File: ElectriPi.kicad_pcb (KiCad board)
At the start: 2 copper layers, 65 x 56 mm, 57 parts, among them IC2 TPS51397ARJER, J1 282837-2, J2 JST XH 01x02, J3 JST XH 01x02, J6 Raspberry_Pi_2_3, J8 JST XH 01x02, Q1 SiA471DJ, Q2 SiA430DJT, U1 LM74700, U2 COOLING, U3 TVS0500DRV

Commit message: Fix libraries and updated back silk
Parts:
- G***: value LOGO -> V3D Logo Small; footprint LOGO -> Logos:V3D Logo Small

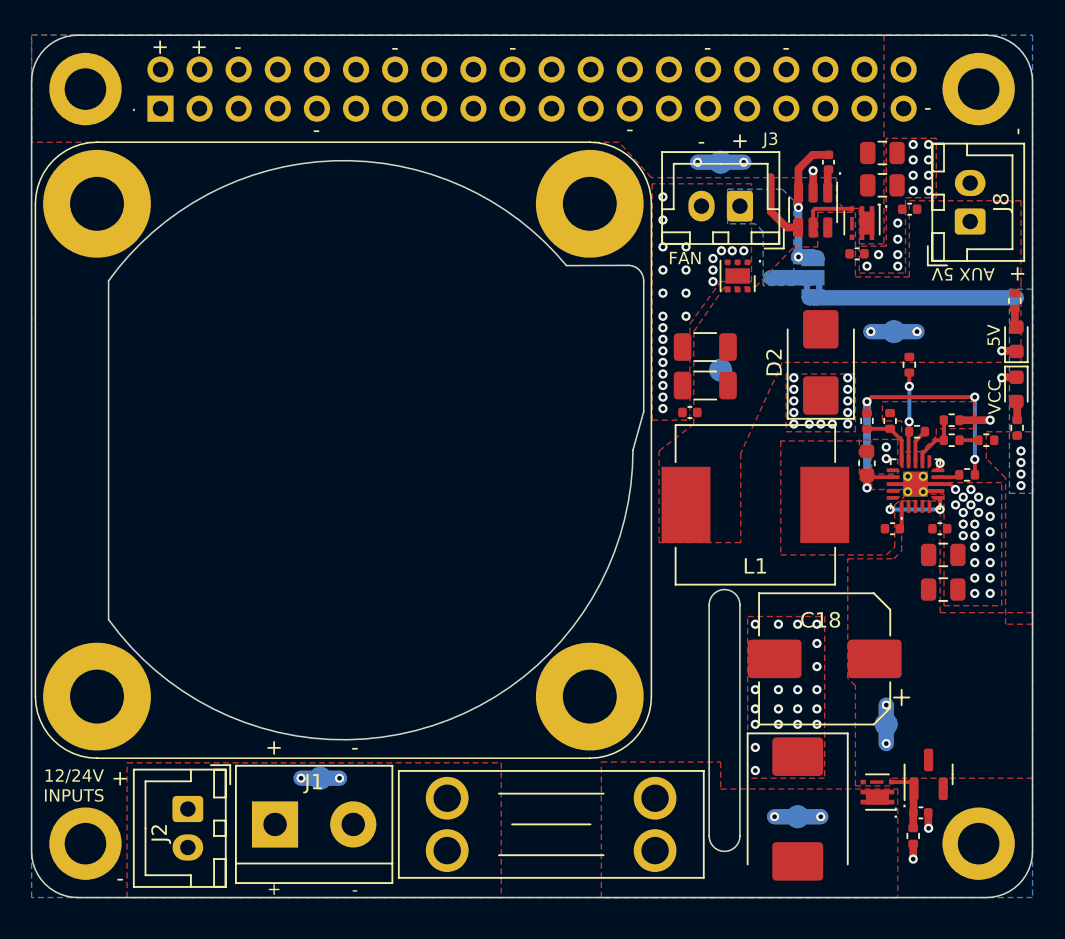
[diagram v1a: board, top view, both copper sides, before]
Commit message: Remove JST input / output connectors! Not rated for currents
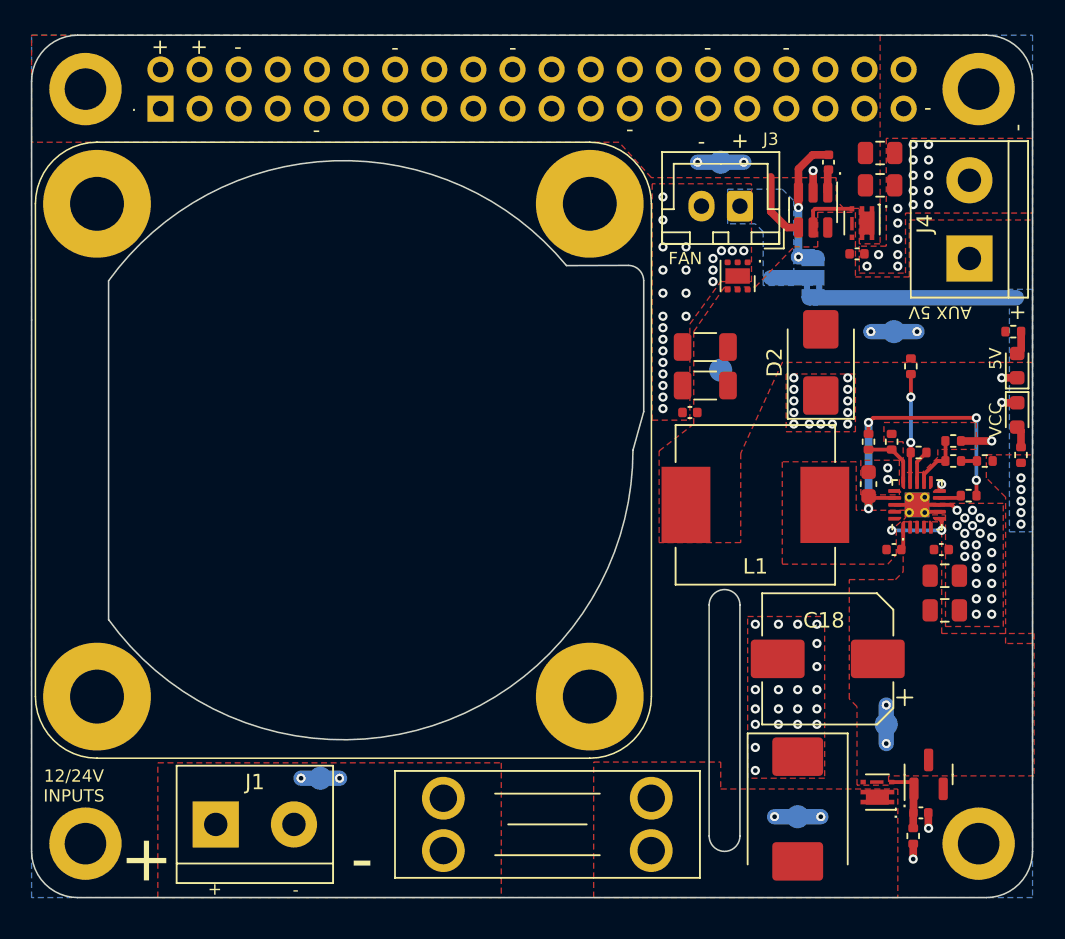
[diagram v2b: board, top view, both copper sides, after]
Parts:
- removed C15: 0.1uF, Capacitor_SMD:C_0402_1005Metric
- removed J2, J8: JST XH 01x02, Connector_JST:JST_XH_B2B-XH-A_1x02_P2.50mm_Vertical
- added J4: 282837-2, TerminalBlock:TerminalBlock_bornier-2_P5.08mm, F.Cu at (146.2, 67.8)
- moved J1 3.85 mm to (97.2, 104.5)
- moved R6 2.00 mm to (149.0, 72.5), turned to 180 degrees
- moved R8 1.78 mm to (149.5, 80.5)
- moved D3 1.71 mm to (149.2, 74.7)
- moved D5 1.66 mm to (149.2, 77.9)
- moved C6 1.35 mm to (144.3, 86.7)
- moved C3 1.35 mm to (139.6, 82.4)
- moved C8 1.35 mm to (141.2, 86.7)
- moved R1 1.35 mm to (147.2, 80.9)
- moved R12 1.35 mm to (146.1, 83.2)
- moved R4 1.35 mm to (139.6, 79.7)
- moved R5 1.35 mm to (141.1, 79.7)
- moved R7 1.35 mm to (145.1, 80.9)
- moved C1 1.35 mm to (144.6, 88.3)
- moved C2 1.35 mm to (144.6, 90.6)
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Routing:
- net FB: track 5.95 -> 7.19 mm
- net GND: track 15.6 -> 15.8 mm, vias 103 -> 106
- net Vin: vias 6 -> 7

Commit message: Updated layout to new ideal diode controller part and passives. Need to regen manf outputs.
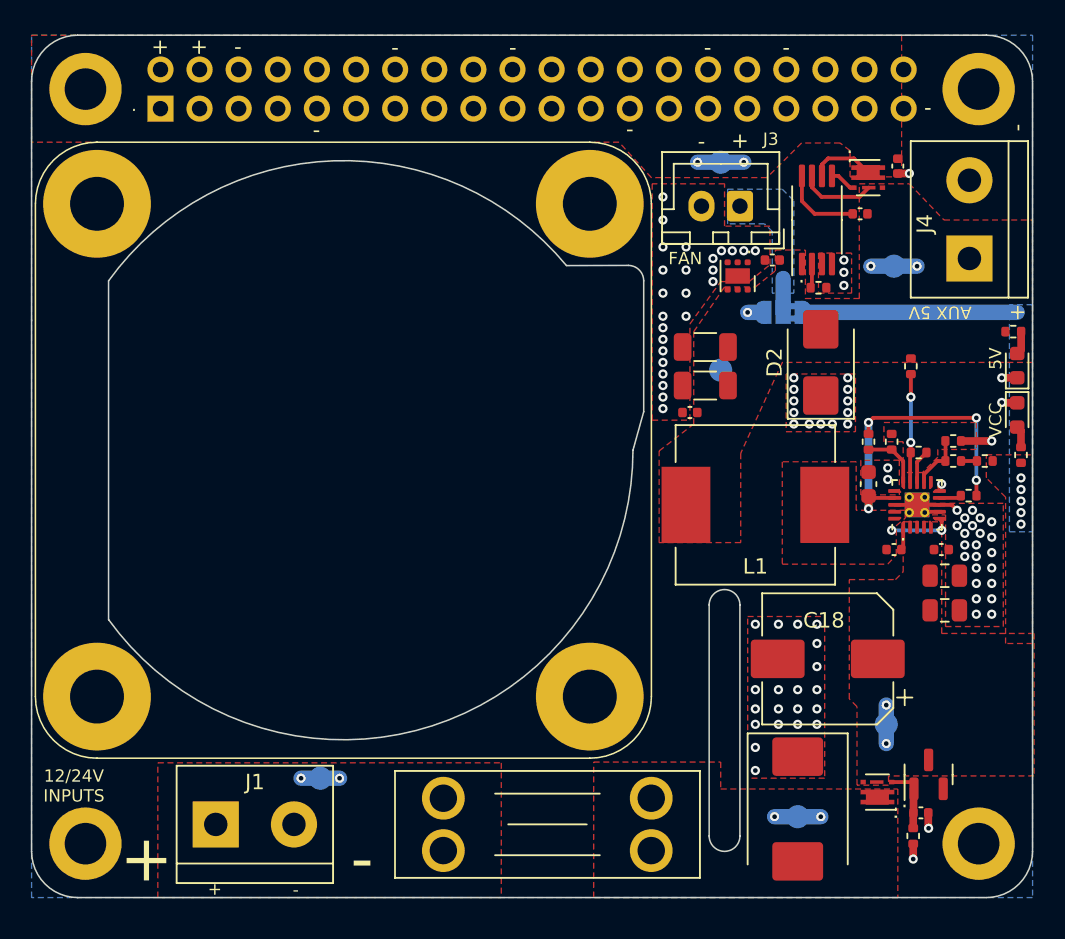
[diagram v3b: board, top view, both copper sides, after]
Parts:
- removed C12: 22 uF, Capacitor_SMD:C_0805_2012Metric
- removed U1: LM74700, Package_TO_SOT_SMD:SOT-23-6
- added R2: 110K, Resistor_SMD:R_0402_1005Metric, F.Cu at (136.3, 69.7)
- added U5: TPS2413PW, Package_SO:TSSOP-8_4.4x3mm_P0.65mm, F.Cu at (136.2, 65.2)
- C11: value 22 uF -> 0.1uF; footprint Capacitor_SMD:C_0805_2012Metric -> Capacitor_SMD:C_0402_1005Metric
- C9: value 0.1uF -> 2200p
- moved C10 5.51 mm to (133.3, 67.8), turned to 180 degrees
- moved TP1 4.25 mm to (141.2, 68.2)
- moved C9 3.93 mm to (139.1, 64.8), turned to 180 degrees
- moved JP1 2.98 mm to (134.1, 71.2), turned to 180 degrees
- moved Q2 2.98 mm to (139.6, 62.5), turned to 0 degrees
- moved C11 1.70 mm to (141.5, 61.8), turned to -90 degrees
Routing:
- net Net-(U5-BYP): track 1.50 -> 5.27 mm
- net +5V: track 12.0 -> 8.93 mm, vias 4 -> 3
- net Net-(Q2-G): track 3.66 -> 1.74 mm
- net Net-(U5-RSET): track 0.00 -> 1.57 mm
- net Vin: track 15.7 -> 16.4 mm
- net GND: track 15.8 -> 15.1 mm, vias 106 -> 93
- net Net-(J3-Pin_1): track 2.75 -> 2.20 mm

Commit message: Rounded tracks
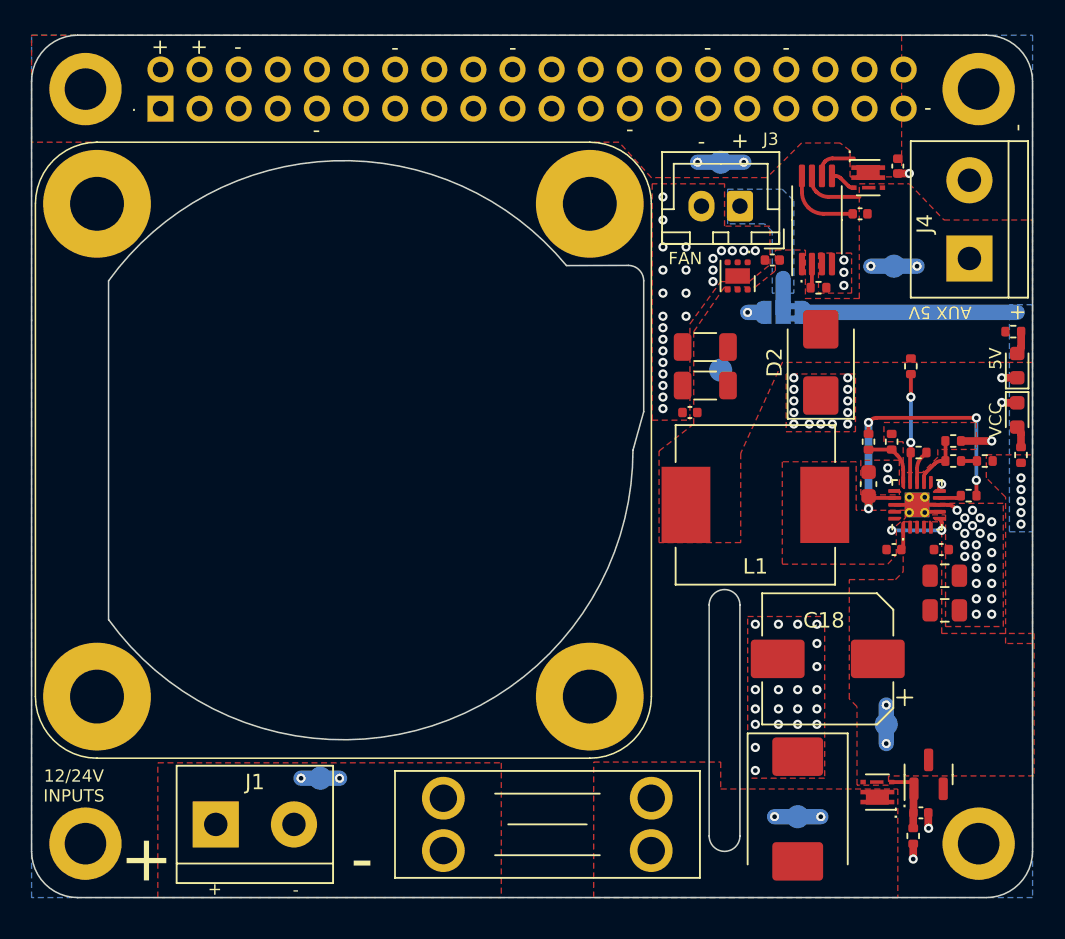
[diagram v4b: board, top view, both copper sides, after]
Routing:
- net 5V_PI: track 7.29 -> 5.91 mm
- net +5V: track 8.93 -> 7.99 mm

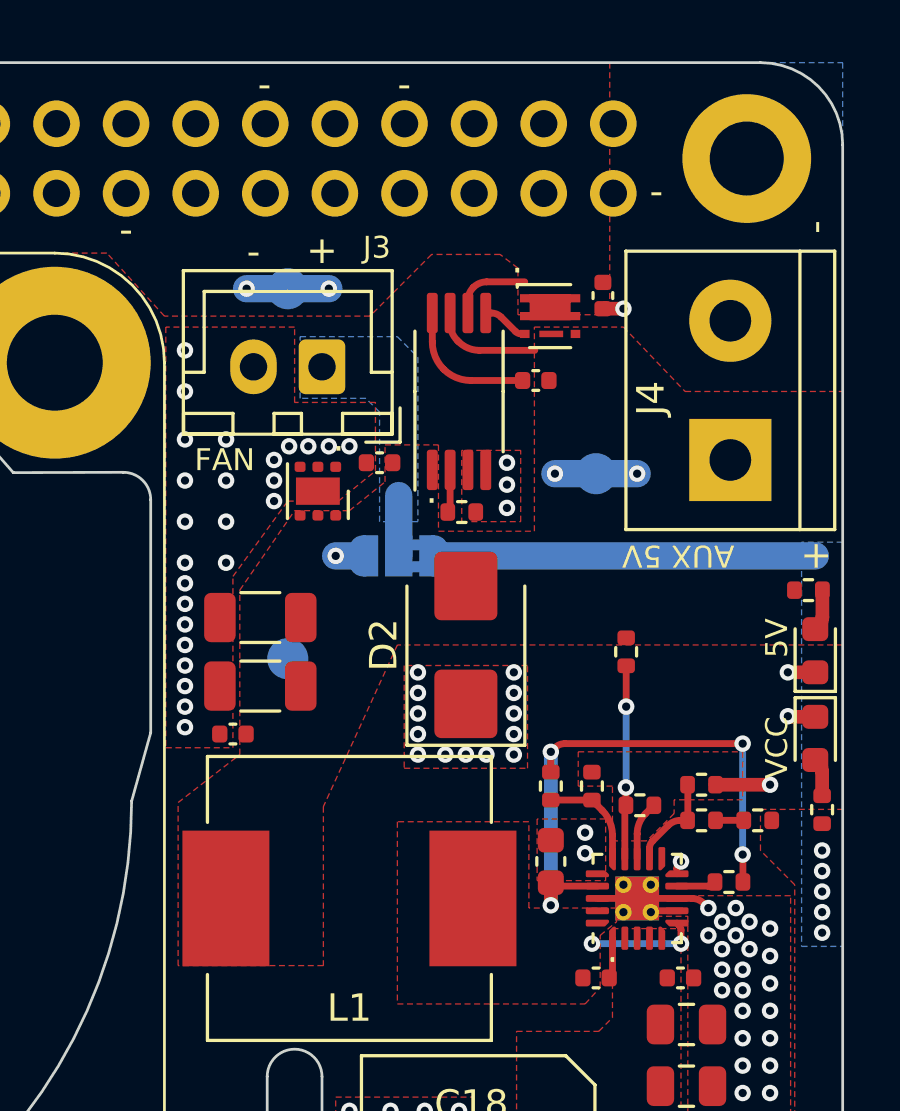
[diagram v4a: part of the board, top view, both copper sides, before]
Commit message: Layout, need manf output regen
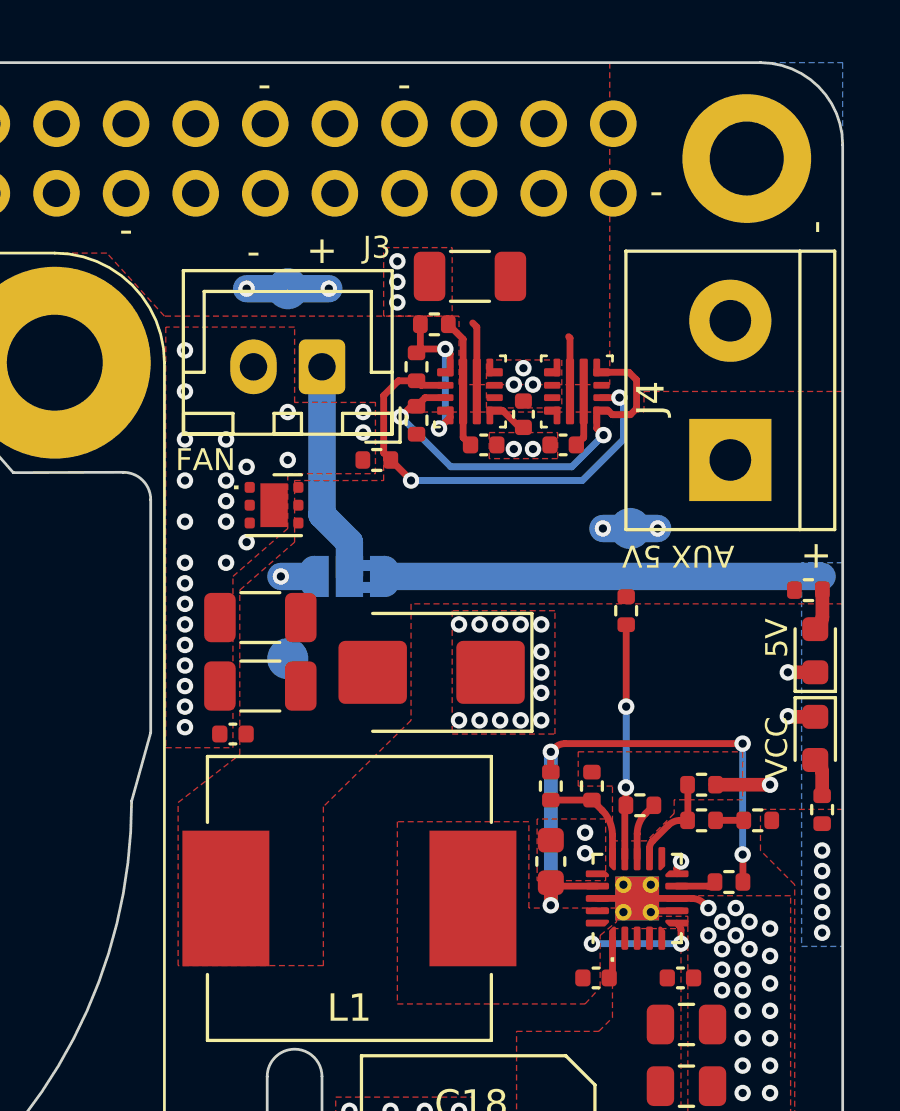
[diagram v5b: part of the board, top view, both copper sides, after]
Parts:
- removed Q2: SiA430DJT, Package_TO_SOT_SMD:Vishay_PowerPAK_SC70-6L_Single
- removed U5: TPS2413PW, Package_SO:TSSOP-8_4.4x3mm_P0.65mm
- added C12: 100uF, Capacitor_SMD:C_1206_3216Metric, F.Cu at (136.7, 61.0)
- added R10: 33K, Resistor_SMD:R_0402_1005Metric, F.Cu at (133.2, 67.8)
- added R15: 110K, Resistor_SMD:R_0402_1005Metric, F.Cu at (135.3, 62.8)
- added R9: 110K, Resistor_SMD:R_0402_1005Metric, F.Cu at (134.7, 66.3)
- added U1: LM73100, RPW0010A:Texas_VQFN-HR-10_2x2mm_P0.475mm, F.Cu at (136.7, 65.2)
- added U4: LM73100, RPW0010A:Texas_VQFN-HR-10_2x2mm_P0.475mm, F.Cu at (140.6, 65.2)
- R2: value 110K -> 33K
- moved C11 5.64 mm to (140.1, 67.2), turned to 180 degrees
- moved R2 5.55 mm to (134.7, 64.3), turned to -90 degrees
- moved C10 3.86 mm to (137.2, 67.2), turned to 0 degrees
- moved TP1 2.36 mm to (142.5, 70.2), turned to 0 degrees
- moved JP1 1.95 mm to (132.2, 72.0)
- moved U3 1.68 mm to (129.5, 69.4), turned to 0 degrees
- moved D2 1.60 mm to (135.2, 75.5), turned to 180 degrees
- moved R13 1.50 mm to (142.3, 73.2)
- moved C9 1.31 mm to (138.6, 66.1), turned to 90 degrees
- moved G*** 1.00 mm to (134.0, 79.2)
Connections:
- C11 pad 1: 5V_PI -> +5V
- C9 pad 1: +5V -> Net-(U1-dVdt)
- C9 pad 2: Net-(U5-BYP) -> GND
- R2 pad 1: Net-(U5-RSET) -> UVLO
- R2 pad 2: GND -> OVLO
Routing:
- net OVLO: track 0.00 -> 16.7 mm, vias 0 -> 2
- net Net-(U1-PG): track 0.00 -> 15.2 mm, vias 0 -> 2
- net UVLO: track 0.00 -> 6.40 mm, vias 0 -> 2
- net Net-(J3-Pin_1): track 2.20 -> 8.06 mm
- net Net-(U5-BYP): track 5.14 -> 0.00 mm
- net Vin: track 16.4 -> 18.4 mm
- net +5V: track 7.99 -> 10.00 mm
- net Net-(Q2-G): track 1.70 -> 0.00 mm
- net 5V_PI: track 5.91 -> 7.58 mm
- net Net-(U5-RSET): track 1.57 -> 0.00 mm
- net FB: track 7.19 -> 8.69 mm
- net Net-(U1-dVdt): track 0.00 -> 1.30 mm
- net GND: track 15.0 -> 14.3 mm, vias 93 -> 97
- removed copper zone on B.Cu, net Net-(J3-Pin_1)

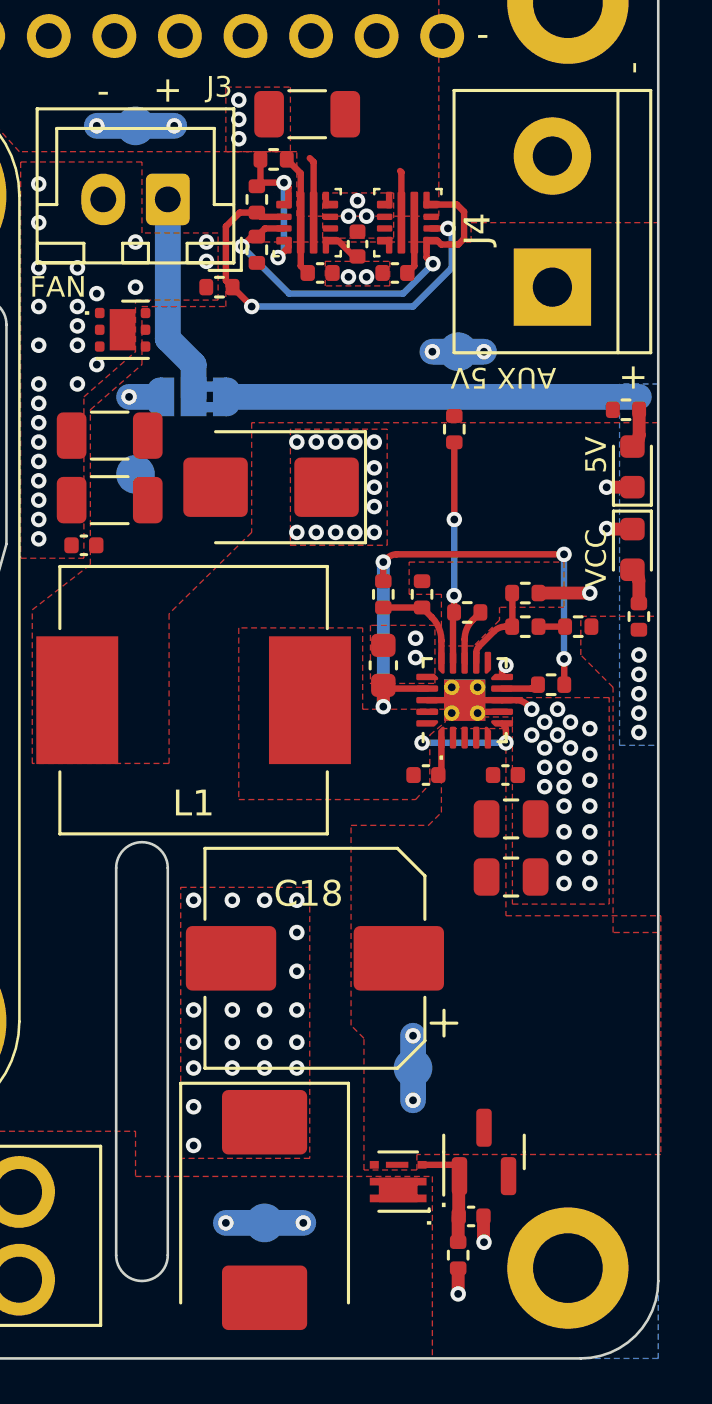
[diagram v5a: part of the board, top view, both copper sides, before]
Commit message: Round tracks
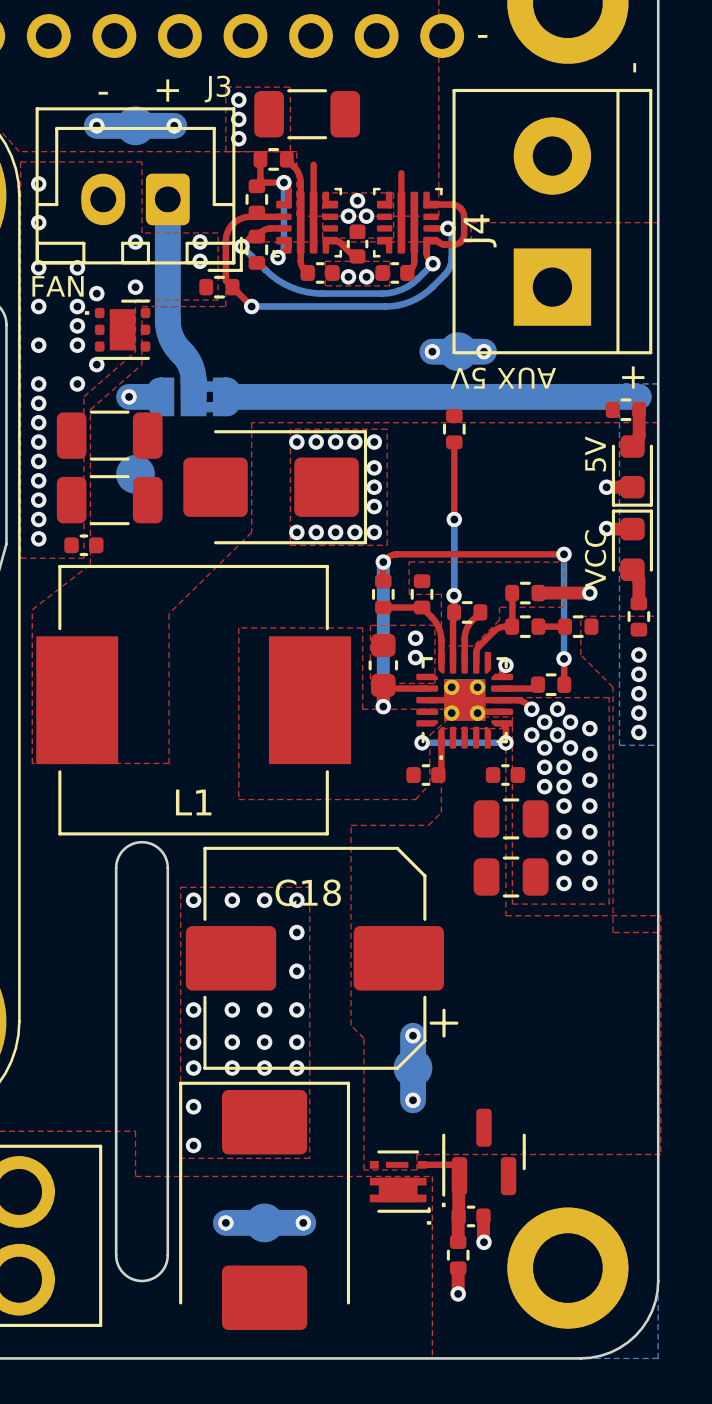
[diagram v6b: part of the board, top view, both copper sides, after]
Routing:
- net OVLO: track 16.7 -> 16.2 mm
